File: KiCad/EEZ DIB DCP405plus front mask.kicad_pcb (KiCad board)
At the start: 2 copper layers, 35 x 111.5 mm, 7 parts

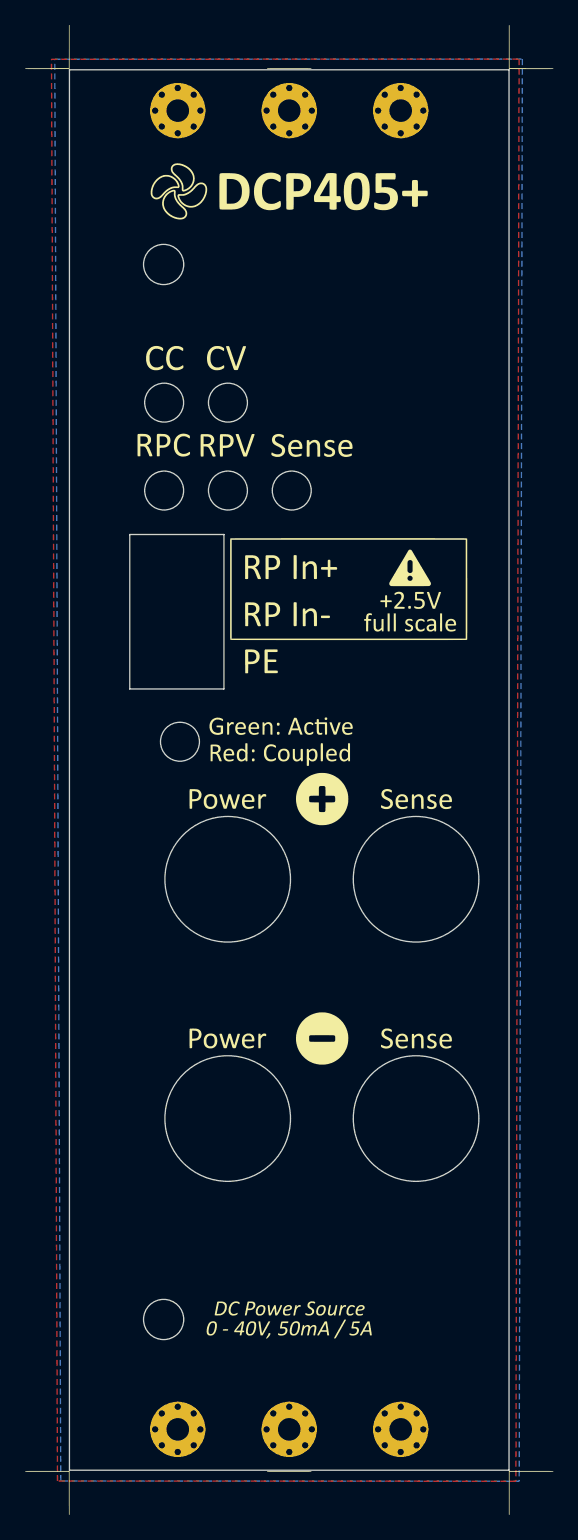
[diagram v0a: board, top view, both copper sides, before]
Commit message: Resized front masks
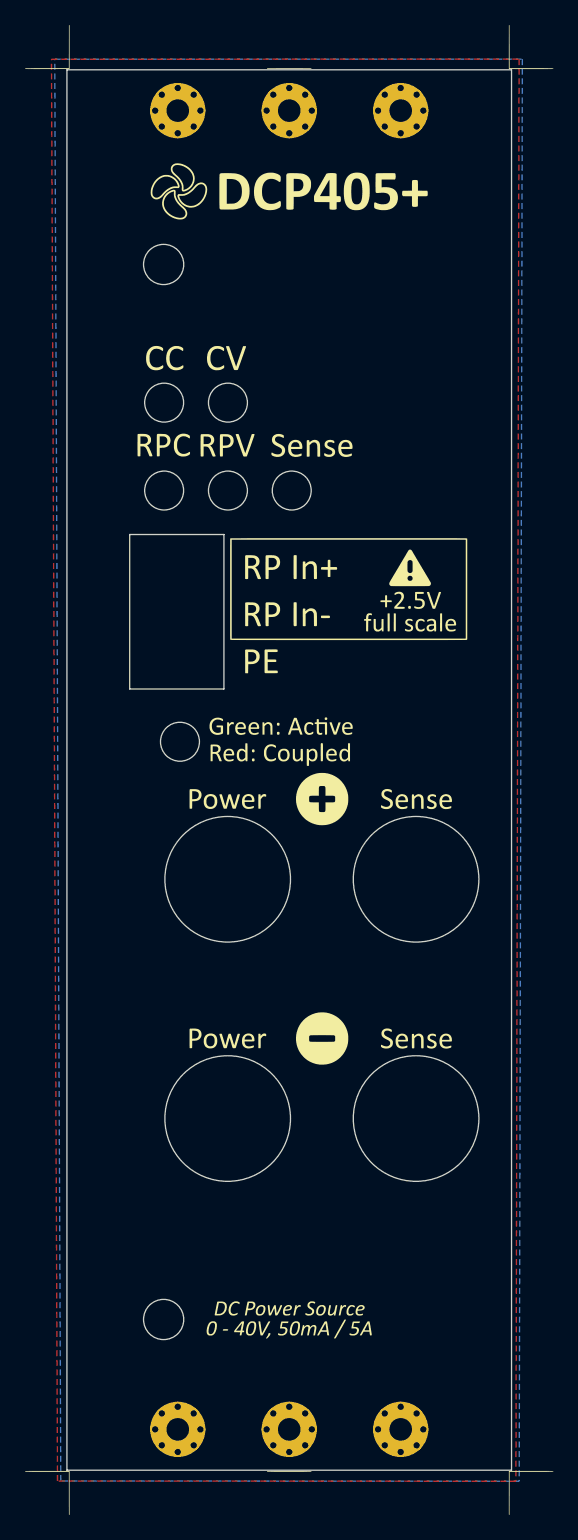
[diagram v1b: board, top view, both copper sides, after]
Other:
- board size 35 x 111.5 mm -> 35.4 x 111.5 mm
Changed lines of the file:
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@@
 			(layer "F.SilkS"
 				(type "Top Silk Screen")
+				(color "Black")
 			)
 			(layer "F.Paste"
@@
 			(layer "F.Mask"
 				(type "Top Solder Mask")
+				(color "White")
 				(thickness 0.01)
 			)
@@
 			(layer "dielectric 1"
 				(type "core")
+				(color "Aluminum")
 				(thickness 1.51)
 				(material "FR4")
@@
 			(layer "B.Mask"
 				(type "Bottom Solder Mask")
+				(color "White")
 				(thickness 0.01)
 			)
@@
 			(layer "B.SilkS"
 				(type "Bottom Silk Screen")
+				(color "Black")
 			)
 			(copper_finish "None")
@@
 		(layer "B.Paste")
 	)
-	(gr_line
-		(start 140.5 150)
-		(end 140.5 38.5)
+	(gr_rect
+		(start 140.3 38.5)
+		(end 175.7 150)
 		(stroke
 			(width 0.05)
-			(type solid)
+			(type default)
 		)
-		(locked yes)
+		(fill no)
 		(layer "Edge.Cuts")
 	)
@@
 		(layer "Edge.Cuts")
 	)
-	(gr_line
-		(start 175.5 38.5)
-		(end 140.5 38.5)
-		(stroke
-			(width 0.05)
-			(type solid)
-		)
-		(locked yes)
-		(layer "Edge.Cuts")
-	)
-	(gr_line
-		(start 175.5 38.5)
-		(end 175.5 150)
-		(stroke
-			(width 0.05)
-			(type solid)
-		)
-		(locked yes)
-		(layer "Edge.Cuts")
-	)
-	(gr_line
-		(start 175.5 150)
-		(end 140.5 150)
-		(stroke
-			(width 0.05)
-			(type solid)
-		)
-		(locked yes)
-		(layer "Edge.Cuts")
-	)
 	(gr_rect
 		(start 143.9 50.7)
@@
 		(layer "User.1")
 		(pts
-			(xy 145.3 80.1) (xy 140.5 80.1)
+			(xy 145.3 80.1) (xy 140.3 80)
 		)
 		(height 1.392499)
@@
 			(keep_text_aligned yes)
 		)
-		(gr_text "4,8"
-			(at 142.9 80.342499 0)
+		(gr_text "5"
+			(at 142.8 80.342499 0)
 			(layer "User.1")
 			(effects
@@
 		(layer "User.1")
 		(pts
-			(xy 140.5 102.5) (xy 153.1 101.95)
+			(xy 140.3 102.5) (xy 153.1 101.95)
 		)
 		(height 2.4)
@@
 			(keep_text_aligned yes)
 		)
-		(gr_text "12,6"
-			(at 146.8 103.75 0)
+		(gr_text "12,8"
+			(at 146.7 103.75 0)
 			(layer "User.1")
 			(effects
@@
 		(layer "User.1")
 		(pts
-			(xy 147.97 53.062499) (xy 140.47 50.752499)
+			(xy 148 54) (xy 140.3 50.8)
 		)
 		(height -3.57)
@@
 			(keep_text_aligned yes)
 		)
-		(gr_text "7,5"
-			(at 144.22 48.342499 0)
+		(gr_text "7,7"
+			(at 144.15 49.28 0)
 			(layer "User.1")
 			(effects
@@
 		(layer "User.1")
 		(pts
-			(xy 140.5 146.3) (xy 158 146.3)
+			(xy 140.3 145.8) (xy 158 146.3)
 		)
 		(height -2.147501)
@@
 			(keep_text_aligned yes)
 		)
-		(gr_text "17,5"
-			(at 149.25 143.002499 0)
+		(gr_text "17,7"
+			(at 149.15 142.502499 0)
 			(layer "User.1")
 			(effects
@@
 		(layer "User.1")
 		(pts
-			(xy 147.999999 64.05) (xy 140.5 65.48)
+			(xy 147.999999 64.05) (xy 140.3 65.4)
 		)
 		(height 3.562499)
@@
 			(keep_text_aligned yes)
 		)
-		(gr_text "7,5"
-			(at 144.249999 66.462499 0)
+		(gr_text "7,7"
+			(at 144.149999 66.462499 0)
 			(layer "User.1")
 			(effects
@@
 		(layer "User.1")
 		(pts
-			(xy 140.5 126.3) (xy 153.1 121)
+			(xy 140.3 126.3) (xy 153.1 121)
 		)
 		(height 1.8)
@@
 			(keep_text_aligned yes)
 		)
-		(gr_text "12,6"
-			(at 146.8 126.95 0)
+		(gr_text "12,8"
+			(at 146.7 126.95 0)
 			(layer "User.1")
 			(effects
@@
 		(layer "User.1")
 		(pts
-			(xy 140.5 152.074999) (xy 175.5 152.05)
+			(xy 140.3 150) (xy 175.7 150)
 		)
 		(height 2.5375)
@@
 			(keep_text_aligned yes)
 		)
-		(gr_text "35"
-			(at 158 153.462499 0)
+		(gr_text "35,4"
+			(at 158 151.3875 0)
 			(layer "User.1")
 			(effects
@@
 		(layer "User.1")
 		(pts
-			(xy 149.3 91) (xy 140.5 91)
+			(xy 149.3 91) (xy 140.3 90.9)
 		)
 		(height 2.6)
@@
 			(keep_text_aligned yes)
 		)
-		(gr_text "8,8"
-			(at 144.9 92.45 0)
+		(gr_text "9"
+			(at 144.8 92.45 0)
 			(layer "User.1")
 			(effects
@@
 		(layer "User.1")
 		(pts
-			(xy 140.47 40.762499) (xy 157.97 40.762499)
+			(xy 140.3 40.9) (xy 158 41.75)
 		)
 		(height 2.89)
@@
 			(units 3)
 			(units_format 0)
-			(precision 2)
+			(precision 3)
 			(suppress_zeroes yes)
 		)
@@
 			(keep_text_aligned yes)
 		)
-		(gr_text "17,5"
-			(at 149.22 42.502499 0)
+		(gr_text "17,7"
+			(at 149.15 42.64 0)
 			(layer "User.1")
 			(effects
@@
 		(layer "User.1")
 		(pts
-			(xy 140.48 137.05) (xy 148 137.05)
+			(xy 140.3 136.7) (xy 148 137.05)
 		)
 		(height -2.897501)
@@
 			(keep_text_aligned yes)
 		)
-		(gr_text "7,52"
-			(at 144.24 133.002499 0)
+		(gr_text "7,7"
+			(at 144.15 132.652499 0)
 			(layer "User.1")
 			(effects
@@
 		(layer "User.1")
 		(pts
-			(xy 148 71.05) (xy 140.53 71.05)
+			(xy 148 71.05) (xy 140.3 71)
 		)
 		(height 2.462499)
@@
 			(keep_text_aligned yes)
 		)
-		(gr_text "7,47"
-			(at 144.265 72.362499 0)
+		(gr_text "7,7"
+			(at 144.15 72.362499 0)
 			(layer "User.1")
 			(effects
@@
 		)
 	)
-	(group ""
-		(locked yes)
-		(members "3bec24fe-9634-410f-ae22-abe963cd70e2" "40c1de93-adce-49ae-ba59-9ddb6a63c44d"
-			"b76af28c-8a19-4f35-81c9-1c72619257bb" "bed9b981-e39a-48df-83b7-bc13756cdbbc"
-		)
-	)
